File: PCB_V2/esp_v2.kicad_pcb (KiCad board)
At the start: 2 copper layers, 86 x 67.5 mm, 13 parts, among them J2 Conn_01x03_Socket, J3 Screw_Terminal_01x02, U1 ESP-32S

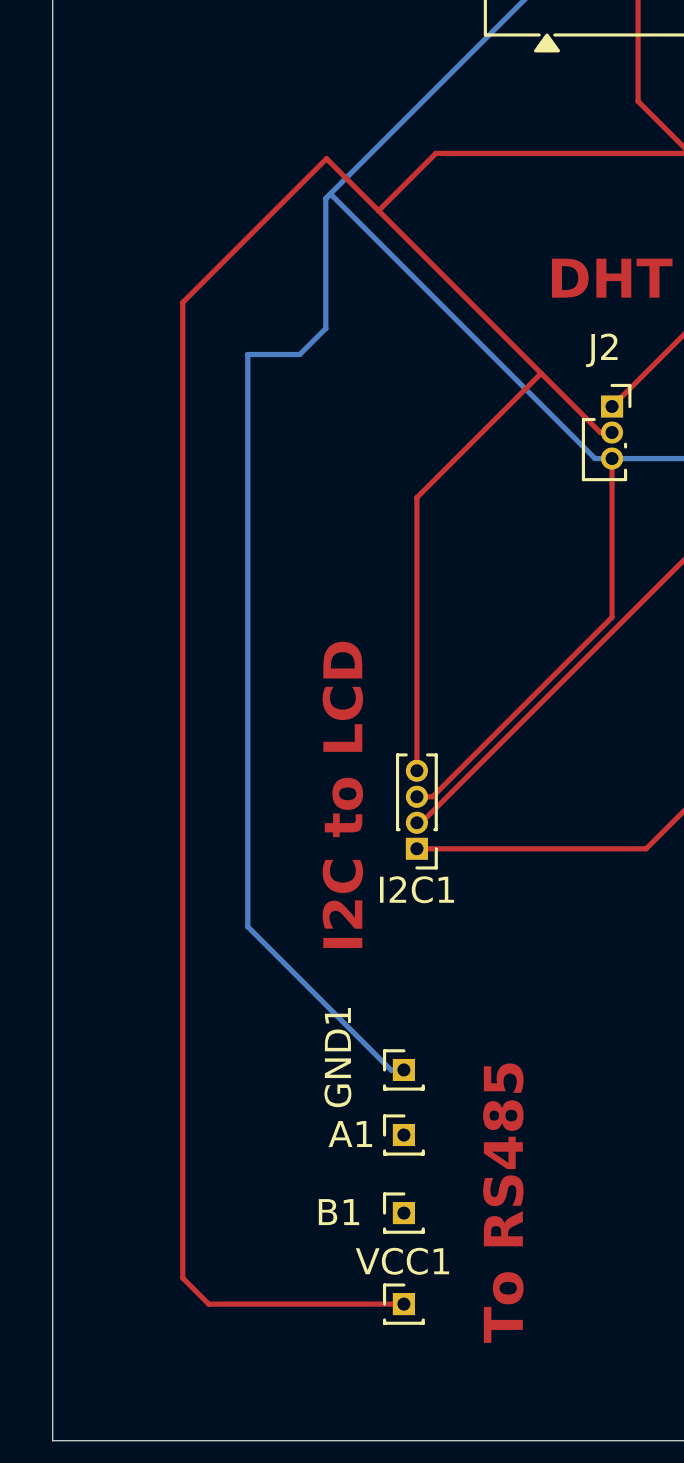
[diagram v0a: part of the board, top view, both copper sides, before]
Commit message: corected the VCC for 7in1
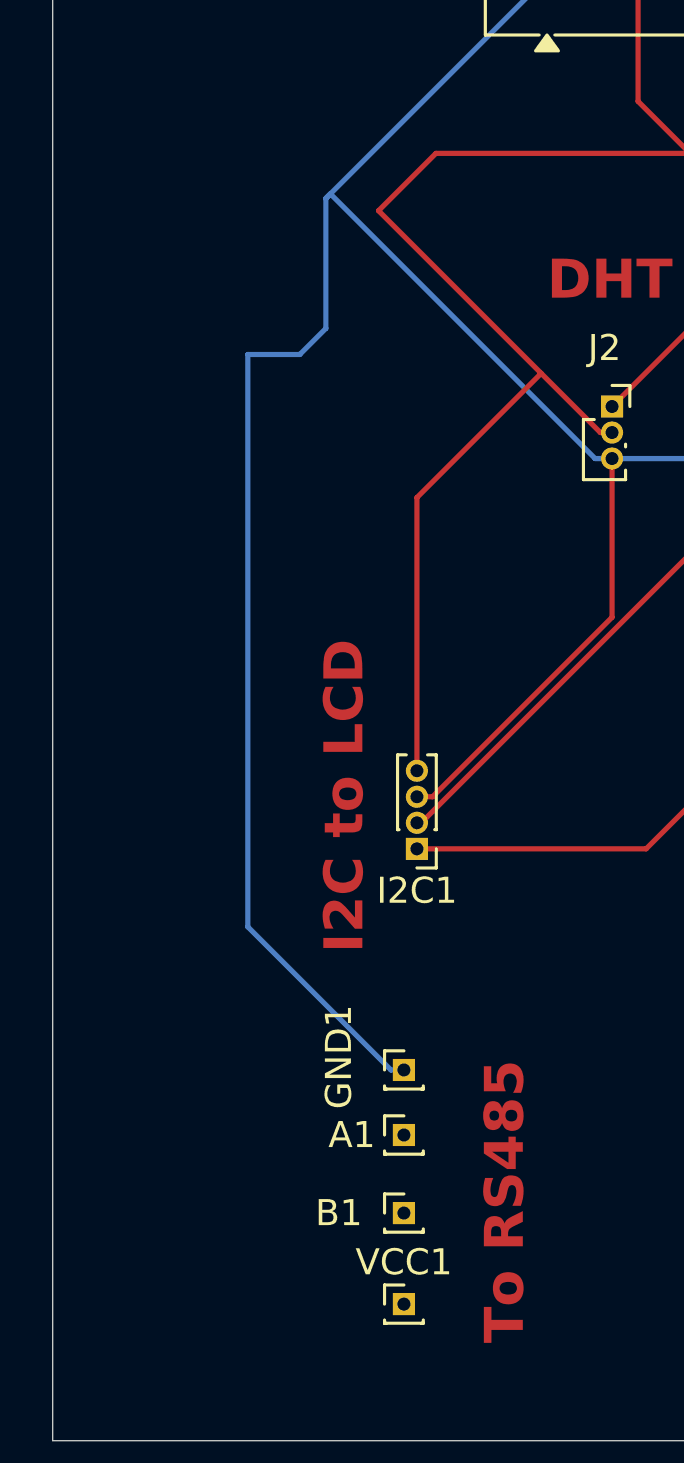
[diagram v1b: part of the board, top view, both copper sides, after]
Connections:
- VCC1 pad 1: VCC -> unconnected-(VCC1-Pin_1-Pad1)
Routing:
- net VCC: track 183.1 -> 126.0 mm
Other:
- board text added: "vcc from 9V"
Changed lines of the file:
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@@
 	(net 38 "unconnected-(U1-IO5-Pad29)")
 	(net 39 "unconnected-(U1-IO2-Pad24)")
+	(net 40 "unconnected-(VCC1-Pin_1-Pad1)")
 	(footprint "Connector_PinHeader_1.00mm:PinHeader_1x01_P1.00mm_Vertical"
 		(layer "F.Cu")
@@
 			(layers "*.Cu" "*.Mask")
 			(remove_unused_layers no)
-			(net 6 "VCC")
+			(net 40 "unconnected-(VCC1-Pin_1-Pad1)")
 			(pinfunction "Pin_1")
 			(pintype "passive")
@@
 		)
 	)
+	(gr_text "vcc from 9V\n"
+		(at 77 122.5 0)
+		(layer "Edge.Cuts")
+		(effects
+			(font
+				(size 1 1)
+				(thickness 0.15)
+			)
+			(justify left bottom)
+		)
+	)
 	(gr_text "Desinged by Kitur"
 		(at 95.5 109 0)
@@
 	)
 	(segment
-		(start 71 119.5)
-		(end 70 118.5)
-		(width 0.2)
-		(layer "F.Cu")
-		(net 6)
-	)
-	(segment
 		(start 106 65)
 		(end 104.5 66.5)
@@
 	)
 	(segment
-		(start 75.525 75.475)
-		(end 77.525 77.475)
-		(width 0.2)
-		(layer "F.Cu")
-		(net 6)
-	)
-	(segment
 		(start 125 63.5)
 		(end 123.5 65)
@@
 	)
 	(segment
-		(start 70 118.5)
-		(end 70 81)
-		(width 0.2)
-		(layer "F.Cu")
-		(net 6)
-	)
-	(segment
 		(start 145 75)
 		(end 136.5 75)
@@
 	)
 	(segment
-		(start 70 81)
-		(end 75.525 75.475)
-		(width 0.2)
-		(layer "F.Cu")
-		(net 6)
-	)
-	(segment
 		(start 104.5 75.27)
 		(end 89.5 75.27)
@@
 		(width 0.2)
 		(layer "F.Cu")
-		(net 6)
-	)
-	(segment
-		(start 78.5 119.5)
-		(end 71 119.5)
-		(width 0.2)
-		(layer "F.Cu")

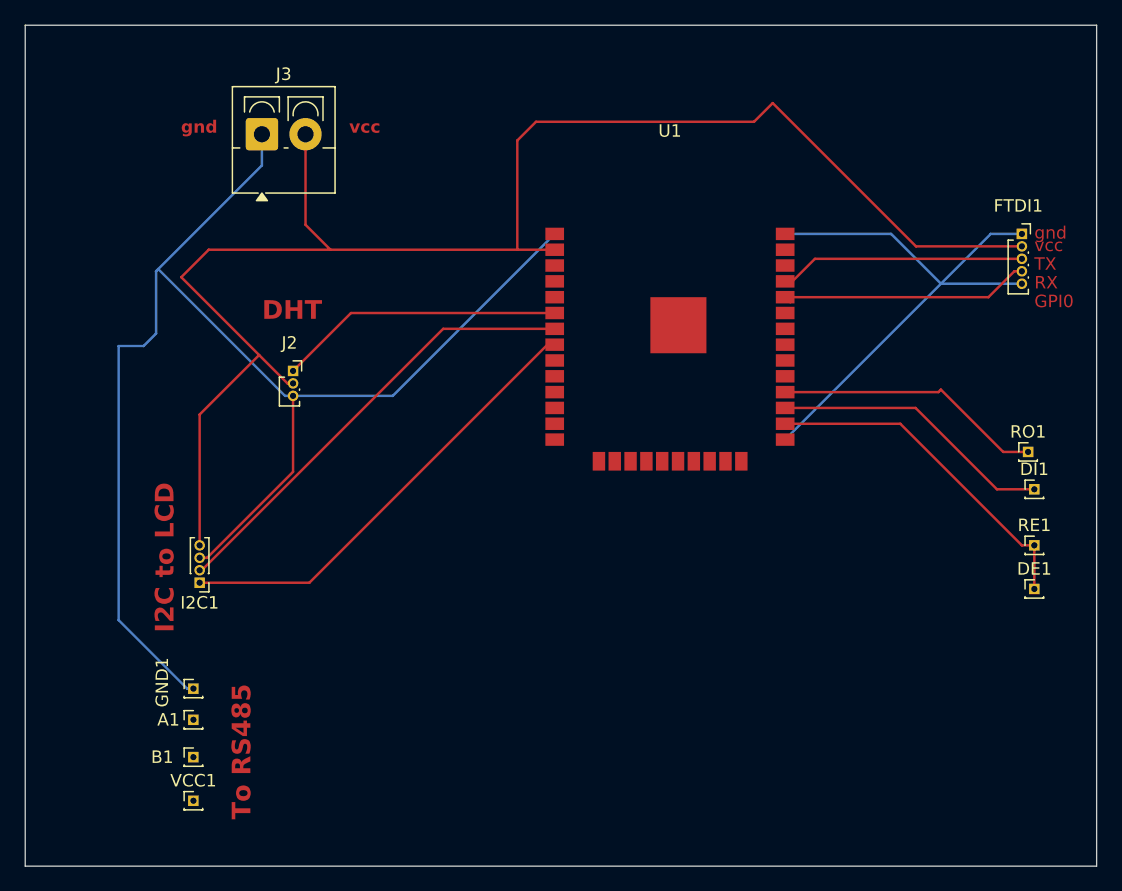
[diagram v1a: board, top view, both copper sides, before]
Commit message: expanded tracks' width
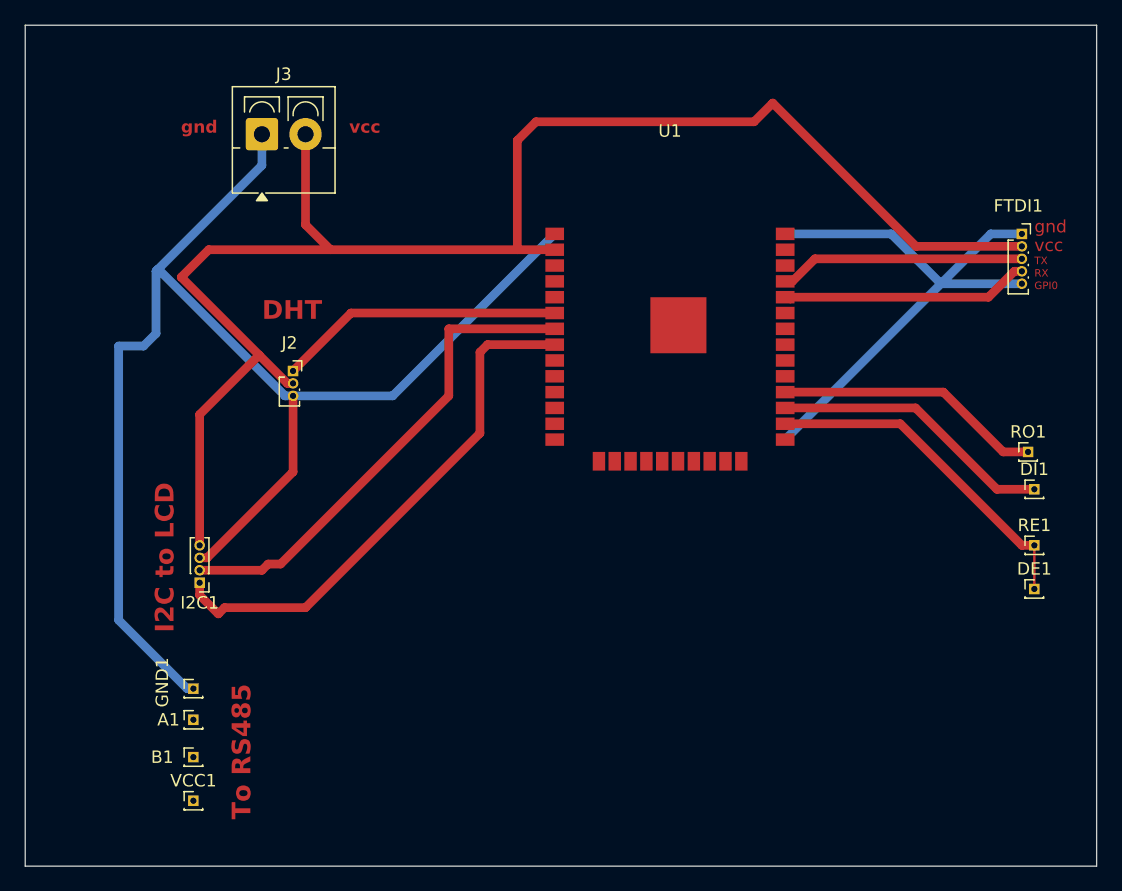
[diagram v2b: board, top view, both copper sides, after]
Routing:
- net Net-(I2C1-Pin_1): track 36.4 -> 43.5 mm
- net Net-(I2C1-Pin_2): track 36.5 -> 39.7 mm

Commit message: After our first etching we reiliaze pins were too small . SO we had toenlearge them.
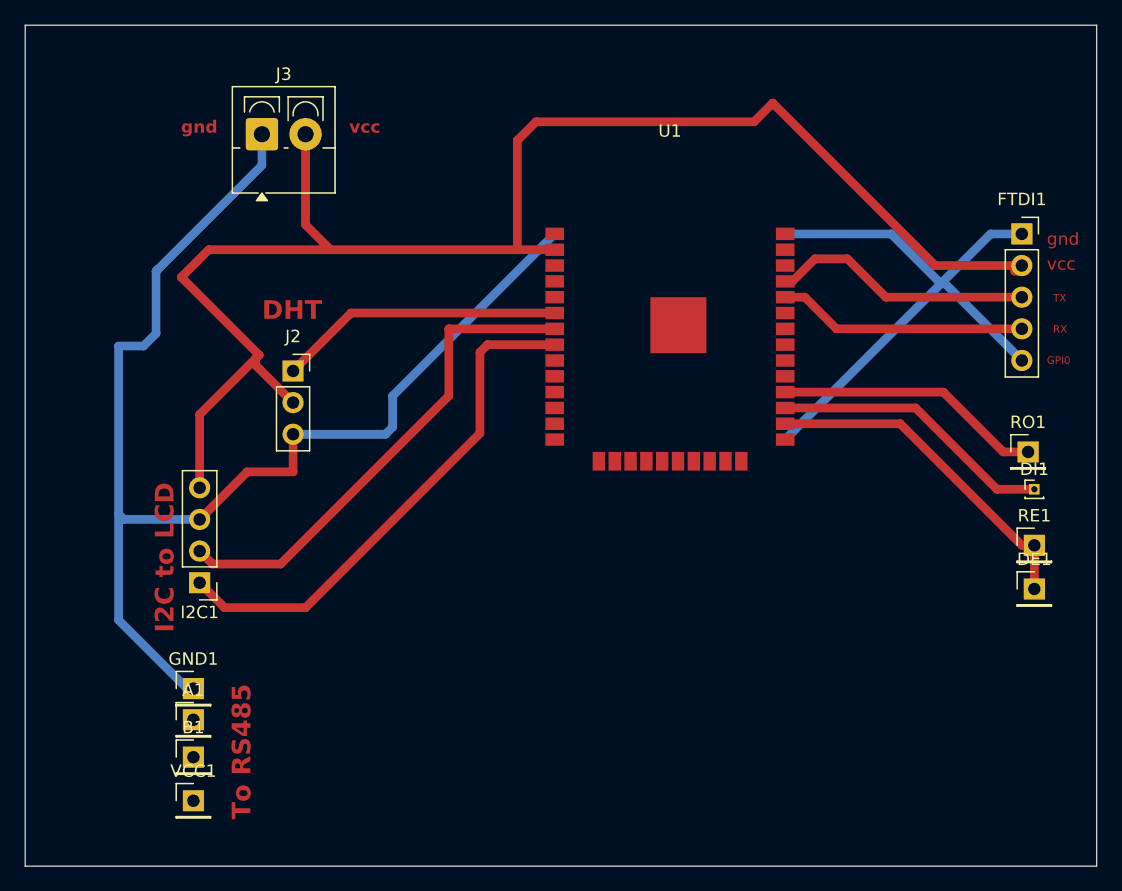
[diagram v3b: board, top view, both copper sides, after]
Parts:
- A1, B1, DE1, GND1, RE1, RO1, VCC1: footprint Connector_PinHeader_1.00mm:PinHeader_1x01_P1.00mm_Vertical -> Connector_PinHeader_2.54mm:PinHeader_1x01_P2.54mm_Vertical
- FTDI1: footprint Connector_PinSocket_1.00mm:PinSocket_1x05_P1.00mm_Vertical -> Connector_PinSocket_2.54mm:PinSocket_1x05_P2.54mm_Vertical
- I2C1: footprint Connector_PinHeader_1.00mm:PinHeader_1x04_P1.00mm_Vertical -> Connector_PinHeader_2.54mm:PinHeader_1x04_P2.54mm_Vertical
- J2: footprint Connector_PinSocket_1.00mm:PinSocket_1x03_P1.00mm_Vertical -> Connector_PinSocket_2.54mm:PinSocket_1x03_P2.54mm_Vertical
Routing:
- net GND: track 111.3 -> 101.4 mm
- net Net-(FTDI1-Pin_1): track 46.5 -> 49.6 mm
- net VCC: track 126.0 -> 124.1 mm
- net Net-(FTDI1-Pin_3): track 19.7 -> 21.0 mm
- net Net-(I2C1-Pin_1): track 43.5 -> 42.5 mm
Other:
- board text added: "Designed by Kitur"
- board text removed: "Desinged by Kitur"

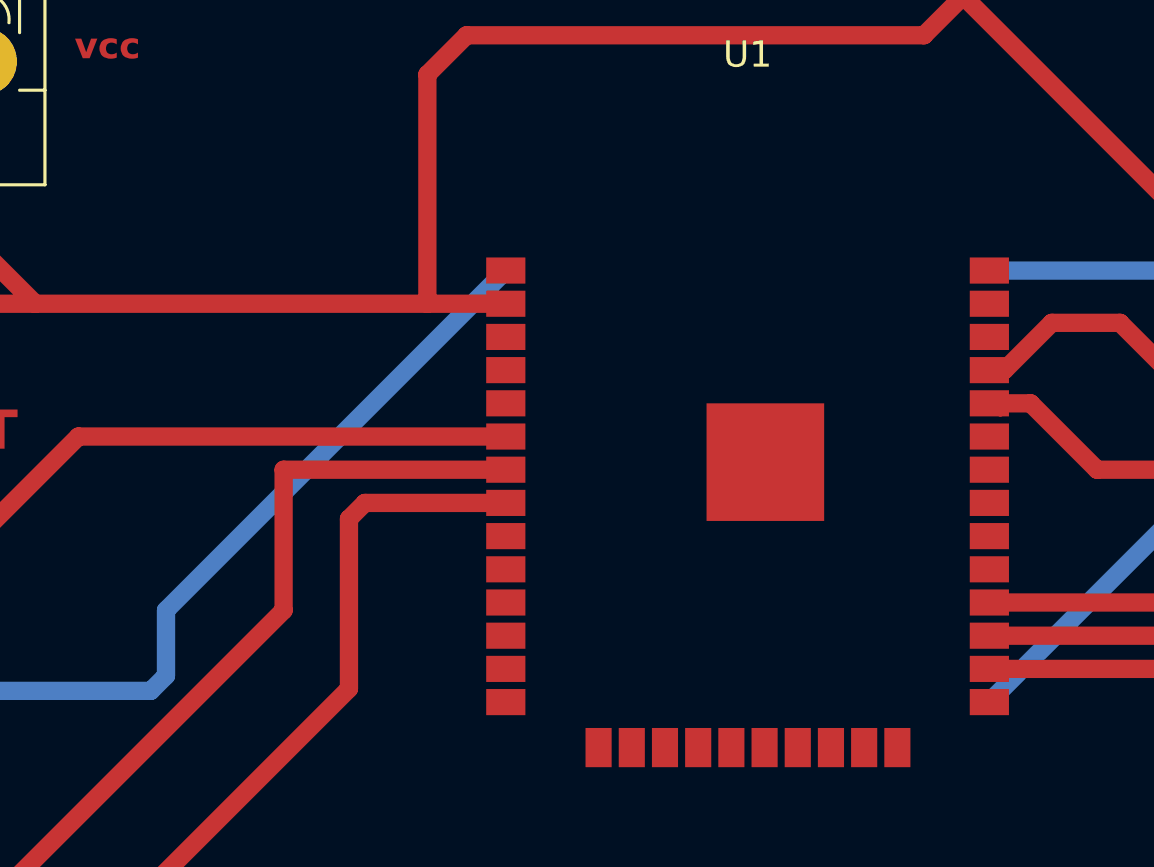
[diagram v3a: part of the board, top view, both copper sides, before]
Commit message: adding vias to mke back connections
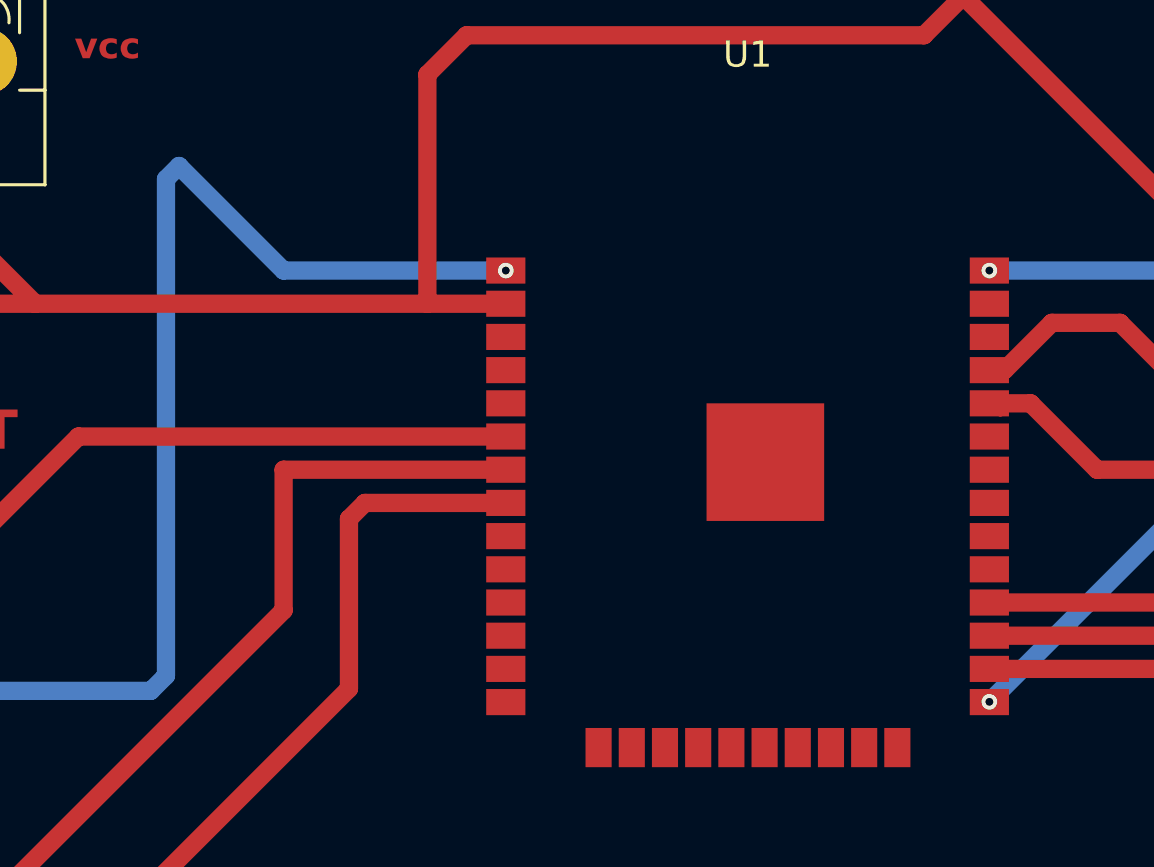
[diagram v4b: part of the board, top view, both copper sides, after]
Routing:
- net GND: track 101.4 -> 114.3 mm, vias 0 -> 1
- net Net-(FTDI1-Pin_1): vias 0 -> 2
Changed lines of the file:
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@@
+		(net 5)
+	)
+	(via
+		(at 107.5 74)
+		(size 0.6)
+		(drill 0.3)
+		(layers "F.Cu" "B.Cu")
 		(net 5)
 	)
@@
 	)
 	(segment
-		(start 94.5 87)
+		(start 99 74)
 		(end 107.5 74)
 		(width 0.7)
@@
 	(segment
 		(start 94.5 89.5)
-		(end 94.5 87)
+		(end 94.5 70.5)
 		(width 0.7)
 		(layer "B.Cu")
@@
 	)
 	(segment
+		(start 95 70)
+		(end 99 74)
+		(width 0.7)
+		(layer "B.Cu")
+		(net 5)
+	)
+	(segment
+		(start 94.5 70.5)
+		(end 95 70)
+		(width 0.7)
+		(layer "B.Cu")
+		(net 5)
+	)
+	(segment
 		(start 83.5 84.54)
 		(end 86.5 87.54)
@@
 		(net 19)
 	)
-	(segment
+	(via
+		(at 126 90.5)
+		(size 0.6)
+		(drill 0.3)
+		(layers "F.Cu" "B.Cu")
+		(net 20)
+	)
+	(via
+		(at 126 74)
+		(size 0.6)
+		(drill 0.3)
+		(layers "F.Cu" "B.Cu")
+		(net 20)
+	)
+	(segment
